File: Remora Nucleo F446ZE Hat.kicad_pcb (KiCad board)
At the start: 2 copper layers, 138 x 162 mm, 174 parts, among them J1 Conn_02x35_Odd_Even, J10 Conn_01x02_Socket, J11 Conn_01x04_Socket, J12 Conn_01x02_Socket, J13 Conn_01x04_Socket, J14 Conn_01x02_Socket, J15 Conn_01x04_Socket, J16 Conn_01x02_Socket, J17 Conn_01x04_Socket, J18 Conn_01x02_Socket, J19 Conn_01x04_Socket, J2 MSD-1-A, J20 Conn_01x04_Socket, J21 Conn_01x02_Socket, J23 Conn_01x04_Socket, J24 Conn_01x04_Socket, J25 Conn_01x04_Socket, J26 Conn_01x04_Socket, J27 Conn_01x02_Socket, J3 UART_TX, J4 Conn_02x35_Odd_Even, J5 24V Logic, J6 24V Peripheral, J7 Conn_01x04_Socket, J8 Conn_01x02_Socket, J9 Conn_01x04_Socket, SW1 SW_Push, U1 Wiznet W5500 Eval Module, U10 LTV-247, U11 LTV-247, U12 AM26LS31CDR, U13 LTV-247, U14 AM26LS31CDR, U19 LTV-247, U2 XL1509-12, U3 XL1509-5.0, U4 LTV-247, U5 AM26LS31CDR, U6 LTV-247, U7 LTV-247, U8 LTV-247, U9 LTV-247

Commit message: Layout work for PSUs
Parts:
- moved R10 411.1 mm to (229.9, 70.2), turned to 90 degrees
- moved D5 406.2 mm to (229.9, 65.3), turned to -90 degrees
- moved D6 368.5 mm to (269.2, 65.2), turned to -90 degrees
- moved J5 284.1 mm to (203.2, 68.2)
- moved C7 281.3 mm to (222.3, 68.2)
- moved U2 276.9 mm to (215.4, 80.0)
- moved C3 274.3 mm to (203.7, 78.6), turned to -90 degrees
- moved C5 266.1 mm to (209.4, 79.9), turned to -90 degrees
- moved JP1 263.7 mm to (223.6, 74.6)
- moved D3 261.7 mm to (214.0, 74.8)
- moved L1 259.2 mm to (214.1, 68.2)
- moved JP3 257.9 mm to (234.3, 66.0), turned to 180 degrees
- moved JP4 257.6 mm to (234.3, 70.4), turned to 180 degrees
- moved J6 255.9 mm to (242.2, 68.3)
- moved C8 247.6 mm to (261.7, 68.3)
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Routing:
- net +24V: track 0.00 -> 60.1 mm
- net VDD: track 0.00 -> 36.6 mm
- net Net-(JP1-A): track 0.00 -> 33.2 mm
- net Net-(JP2-A): track 0.00 -> 32.7 mm
- net Net-(D4-K): track 0.00 -> 13.8 mm
- net Net-(D3-K): track 0.00 -> 13.8 mm
- net +5VD: track 0.00 -> 6.85 mm
- net +12V: track 0.00 -> 6.82 mm
- net Net-(D6-A): track 0.00 -> 1.91 mm
- net Net-(D5-A): track 0.00 -> 1.91 mm
- net GNDREF: vias 9 -> 17
- net GNDPWR: vias 0 -> 9
- added copper zone on B.Cu, net GNDPWR
- added copper zone on F.Cu, net GNDPWR
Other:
- board text added: "24V Isolated"
- board text added: "24V Logic"

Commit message: Added Analog inputs, updates to readme re powering board from external supply
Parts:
- added C27: 100nF, Capacitor_SMD:C_1206_3216Metric_Pad1.33x1.80mm_HandSolder, F.Cu at (315.6, 112.9)
- added C28: 100nF, Capacitor_SMD:C_1206_3216Metric_Pad1.33x1.80mm_HandSolder, F.Cu at (315.6, 116.3)
- added C29: 100nF, Capacitor_SMD:C_1206_3216Metric_Pad1.33x1.80mm_HandSolder, F.Cu at (315.6, 119.6)
- added D7: 5.6V Zener, Package_TO_SOT_SMD:SOT-23, F.Cu at (327.0, 113.6)
- added D8: 5.6V Zener, Package_TO_SOT_SMD:SOT-23, F.Cu at (327.0, 118.3)
- added F10: PRG18BB330MB1RB, Fuse:Fuse_0603_1608Metric_Pad1.05x0.95mm_HandSolder, F.Cu at (331.6, 115.0)
- added F9: PRG18BB330MB1RB, Fuse:Fuse_0603_1608Metric_Pad1.05x0.95mm_HandSolder, F.Cu at (331.6, 112.5)
- added J19: Conn_01x04_Socket, Amphenol QT:QT04ADP83V0000G, F.Cu at (317.7, 104.1)
- added R80: 2K4, Resistor_SMD:R_1206_3216Metric_Pad1.30x1.75mm_HandSolder, F.Cu at (321.6, 112.9)
- added R81: 2K4, Resistor_SMD:R_1206_3216Metric_Pad1.30x1.75mm_HandSolder, F.Cu at (321.6, 116.2)
- added R82: 4K7, Resistor_SMD:R_1206_3216Metric_Pad1.30x1.75mm_HandSolder, F.Cu at (321.6, 119.5)
- added R83: 4K7, Resistor_SMD:R_1206_3216Metric_Pad1.30x1.75mm_HandSolder, F.Cu at (321.6, 122.8)
- added U15: MCP6042, Package_SO:SOIC-8_3.9x4.9mm_P1.27mm, F.Cu at (335.0, 128.1)
- J6: value 24V Peripheral -> 24V Isolated
- JP3: value Peripheral->Logic VDD Jumper -> Isolated->Logic VDD Jumper
- JP4: value Peripheral->Logic GND Jumper -> Isolated->Logic GND Jumper
- moved R1 361.0 mm to (159.7, 88.3), turned to 180 degrees
- moved D2 347.6 mm to (226.7, 105.8)
- moved J3 345.1 mm to (229.2, 110.5), turned to -90 degrees
- moved R2 315.1 mm to (214.0, 187.7), turned to -90 degrees
- moved R68 300.0 mm to (471.8, 304.4)
- moved R69 300.0 mm to (471.8, 307.7)
- moved R70 300.0 mm to (471.8, 311.0)
- moved R71 300.0 mm to (471.8, 314.4)
- moved R3 291.1 mm to (229.2, 105.8), turned to 90 degrees
- moved R79 285.5 mm to (525.9, 314.6)
- moved R77 282.3 mm to (525.9, 307.9)
- moved R78 280.6 mm to (525.9, 311.3)
- moved R75 279.1 mm to (525.9, 301.3)
- moved R76 277.4 mm to (525.9, 304.6)
- moved R73 276.0 mm to (525.9, 294.7)
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- renumbered C27 to C30, C29 to C32, J19 to J20, J20 to J21, J21 to J22, J23 to J24, J24 to J25, J25 to J26, J26 to J27, J27 to J28, R84 to R88, R85 to R89, R86 to R90, R87 to R91, U19 to U20
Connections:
- J4 pad 35: unconnected-(J4-Pin_35-Pad35) -> MCU_ANALOG_IN_0
- J4 pad 37: unconnected-(J4-Pin_37-Pad37) -> MCU_ANALOG_IN_1
- R32 pad 1: /Digital Inputs/Digital Input 4-7/INPUT4 -> +5VD
- R33 pad 1: /Digital Inputs/Digital Input 4-7/INPUT5 -> +5VD
- R34 pad 1: /Digital Inputs/Digital Input 4-7/INPUT6 -> +5VD
- R35 pad 1: /Digital Inputs/Digital Input 4-7/INPUT7 -> +5VD
- R40 pad 1: /Digital Inputs/Digital Input 8-11/INPUT8 -> +5VD
- R41 pad 1: /Digital Inputs/Digital Input 8-11/INPUT9 -> +5VD
- R42 pad 1: /Digital Inputs/Digital Input 8-11/INPUT10 -> +5VD
- R43 pad 1: /Digital Inputs/Digital Input 8-11/INPUT11 -> +5VD
- R44 pad 1: /Digital Inputs/Digital Input 12-15/INPUT12 -> +5VD
- R45 pad 1: /Digital Inputs/Digital Input 12-15/INPUT13 -> +5VD
- R46 pad 1: /Digital Inputs/Digital Input 12-15/INPUT14 -> +5VD
- R47 pad 1: /Digital Inputs/Digital Input 12-15/INPUT15 -> +5VD
- R88 pad 1: /Digital Inputs/Digital Input 0-3/INPUT0 -> +5VD
- R89 pad 1: /Digital Inputs/Digital Input 0-3/INPUT1 -> +5VD
- R90 pad 1: /Digital Inputs/Digital Input 0-3/INPUT2 -> +5VD
- R91 pad 1: /Digital Inputs/Digital Input 0-3/INPUT3 -> +5VD
- U10 pad 2: GNDPWR -> /Digital Inputs/Digital Input 12-15/INPUT12
- U10 pad 4: GNDPWR -> /Digital Inputs/Digital Input 12-15/INPUT13
- U10 pad 6: GNDPWR -> /Digital Inputs/Digital Input 12-15/INPUT14
- U10 pad 8: GNDPWR -> /Digital Inputs/Digital Input 12-15/INPUT15
- U20 pad 2: GNDPWR -> /Digital Inputs/Digital Input 0-3/INPUT0
- U20 pad 4: GNDPWR -> /Digital Inputs/Digital Input 0-3/INPUT1
- U20 pad 6: GNDPWR -> /Digital Inputs/Digital Input 0-3/INPUT2
- U20 pad 8: GNDPWR -> /Digital Inputs/Digital Input 0-3/INPUT3
- U7 pad 2: GNDPWR -> /Digital Inputs/Digital Input 4-7/INPUT4
- U7 pad 4: GNDPWR -> /Digital Inputs/Digital Input 4-7/INPUT5
- U7 pad 6: GNDPWR -> /Digital Inputs/Digital Input 4-7/INPUT6
- U7 pad 8: GNDPWR -> /Digital Inputs/Digital Input 4-7/INPUT7
- U9 pad 2: GNDPWR -> /Digital Inputs/Digital Input 8-11/INPUT8
- U9 pad 4: GNDPWR -> /Digital Inputs/Digital Input 8-11/INPUT9
- U9 pad 6: GNDPWR -> /Digital Inputs/Digital Input 8-11/INPUT10
- U9 pad 8: GNDPWR -> /Digital Inputs/Digital Input 8-11/INPUT11
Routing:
- net +3V3: vias 1 -> 0
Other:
- board text added: "Nucleo CNC controller V1"
- board text added: "RESET"
- board text removed: "Remora Nucleo CNC controller V1"

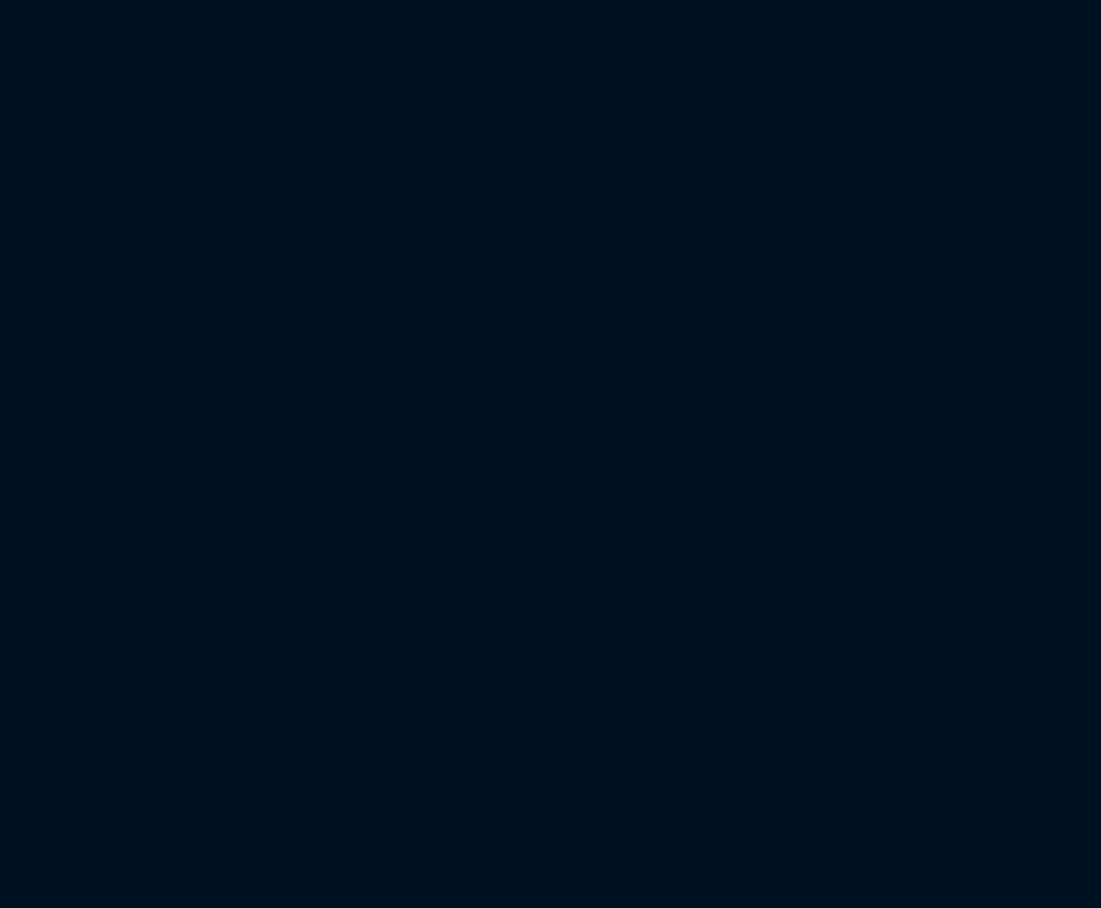
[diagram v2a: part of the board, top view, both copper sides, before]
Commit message: Finalised Spindle DAC, working as expected
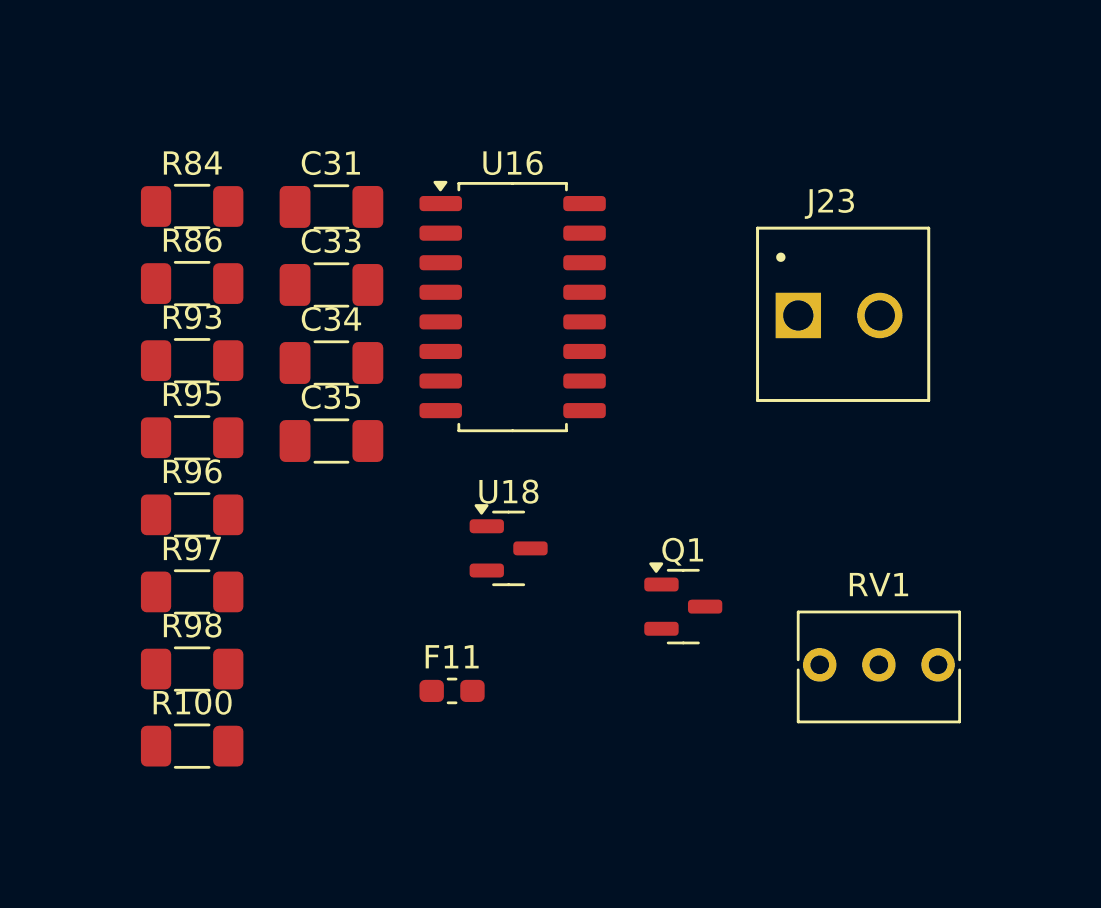
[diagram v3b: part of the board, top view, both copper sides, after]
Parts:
- added C31: 100nF, Capacitor_SMD:C_1206_3216Metric_Pad1.33x1.80mm_HandSolder, F.Cu at (319.0, 37.8)
- added C33: 100nF, Capacitor_SMD:C_1206_3216Metric_Pad1.33x1.80mm_HandSolder, F.Cu at (319.0, 41.2)
- added C34: 100nF, Capacitor_SMD:C_1206_3216Metric_Pad1.33x1.80mm_HandSolder, F.Cu at (319.0, 44.5)
- added C35: 100nF, Capacitor_SMD:C_1206_3216Metric_Pad1.33x1.80mm_HandSolder, F.Cu at (319.0, 47.9)
- added F11: PRG18BB330MB1RB, Fuse:Fuse_0603_1608Metric_Pad1.05x0.95mm_HandSolder, F.Cu at (324.1, 58.6)
- added J23: Spindle Out, EBWA_02_A:ADAMTECH_EBWA-02-A, F.Cu at (340.8, 42.5)
- added Q1: BC847, Package_TO_SOT_SMD:SOT-23, F.Cu at (334.1, 55.0)
- added R100: 4K7, Resistor_SMD:R_1206_3216Metric_Pad1.30x1.75mm_HandSolder, F.Cu at (313.0, 61.0)
- added R84: 180R, Resistor_SMD:R_1206_3216Metric_Pad1.30x1.75mm_HandSolder, F.Cu at (313.0, 37.8)
- added R86: 1K2, Resistor_SMD:R_1206_3216Metric_Pad1.30x1.75mm_HandSolder, F.Cu at (313.0, 41.1)
- added R93: 10K, Resistor_SMD:R_1206_3216Metric_Pad1.30x1.75mm_HandSolder, F.Cu at (313.0, 44.4)
- added R95: 1K2, Resistor_SMD:R_1206_3216Metric_Pad1.30x1.75mm_HandSolder, F.Cu at (313.0, 47.8)
- added R96: 4K7, Resistor_SMD:R_1206_3216Metric_Pad1.30x1.75mm_HandSolder, F.Cu at (313.0, 51.1)
- added R97: 4K7, Resistor_SMD:R_1206_3216Metric_Pad1.30x1.75mm_HandSolder, F.Cu at (313.0, 54.4)
- added R98: 4K7, Resistor_SMD:R_1206_3216Metric_Pad1.30x1.75mm_HandSolder, F.Cu at (313.0, 57.7)
- added RV1: 10K 25 turn trimpot, Potentiometer_THT:Potentiometer_Bourns_3266Y_Vertical, F.Cu at (345.0, 57.5)
- added U16: LTV-247, Package_SO:SOP-16_4.4x10.4mm_P1.27mm, F.Cu at (326.7, 42.1)
- added U18: TL431A, Package_TO_SOT_SMD:SOT-23, F.Cu at (326.6, 52.5)
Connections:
- net test renamed Net-(D7-K)
- J4 pad 43: unconnected-(J4-Pin_43-Pad43) -> MCU_SPINDLE

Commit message: Testing multi channel layout, test layout for stepper drivers
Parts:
- added C36: 100nF, Capacitor_SMD:C_1206_3216Metric_Pad1.33x1.80mm_HandSolder, F.Cu at (235.9, -36.7)
- added C37: 100nF, Capacitor_SMD:C_1206_3216Metric_Pad1.33x1.80mm_HandSolder, F.Cu at (235.9, -33.4)
- added C38: 100nF, Capacitor_SMD:C_1206_3216Metric_Pad1.33x1.80mm_HandSolder, F.Cu at (235.9, -30.0)
- added J20: Conn_01x04_Socket, Amphenol QT:QT04ADP83V0000G, F.Cu at (215.4, -45.5)
- added J21: Conn_01x02_Socket, Amphenol QT:QT02ADP83V0000G, F.Cu at (215.4, -29.4)
- added R84: 1K2, Resistor_SMD:R_1206_3216Metric_Pad1.30x1.75mm_HandSolder, F.Cu at (236.4, -52.8)
- added R85: 1K2, Resistor_SMD:R_1206_3216Metric_Pad1.30x1.75mm_HandSolder, F.Cu at (236.4, -49.5)
- added R86: 1K2, Resistor_SMD:R_1206_3216Metric_Pad1.30x1.75mm_HandSolder, F.Cu at (236.4, -46.2)
- added U16: LTV-247, Package_SO:SOP-16_4.4x10.4mm_P1.27mm, F.Cu at (228.2, -32.4)
- moved J15 134.2 mm to (568.5, 334.2)
- moved J16 134.2 mm to (568.5, 354.2)
- moved J17 133.3 mm to (588.0, 357.4)
- moved J18 133.3 mm to (588.0, 337.4)
- moved C21 130.2 mm to (591.7, 366.0), turned to 180 degrees
- moved R68 125.8 mm to (580.5, 367.7), turned to 180 degrees
- moved R69 125.8 mm to (580.5, 371.0), turned to 180 degrees
- moved R70 125.8 mm to (580.5, 374.3), turned to 180 degrees
- moved R71 125.8 mm to (580.5, 377.6), turned to 180 degrees
- moved R64 121.6 mm to (566.3, 367.7)
- moved R65 121.6 mm to (566.3, 371.0)
- moved R66 121.6 mm to (566.3, 374.3)
- moved R67 121.6 mm to (566.3, 377.6)
- moved C15 121.6 mm to (591.9, 287.1), turned to 180 degrees
- moved U13 121.6 mm to (573.5, 372.6)
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- renumbered C33 to C32, C35 to C33, C32 to C35, J20 to J22, J21 to J23, J22 to J24, J23 to J25, J24 to J26, J25 to J27, J26 to J28, J27 to J29, J28 to J30, R84 to R87, R97 to R88, R96 to R89, R98 to R90, R93 to R91, R95 to R92, R100 to R93, R86 to R94, R88 to R95, R89 to R96, R90 to R97, R91 to R98, U16 to U17, U20 to U19
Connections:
- J4 pad 19: unconnected-(J4-Pin_19-Pad19) -> QEI_B
- J4 pad 21: MCU_DIGITAL_OUT_5 -> unconnected-(J4-Pin_21-Pad21)
- J4 pad 23: MCU_DIGITAL_OUT_4 -> QEI_Z
- J4 pad 25: unconnected-(J4-Pin_25-Pad25) -> MCU_DIGITAL_OUT_5
- J4 pad 27: unconnected-(J4-Pin_27-Pad27) -> MCU_DIGITAL_OUT_4
- J4 pad 4: unconnected-(J4-Pin_4-Pad4) -> QEI_A
- R96 pad 2: Net-(R89-Pad2) -> Net-(R96-Pad2)
- R97 pad 2: Net-(R90-Pad2) -> Net-(R97-Pad2)
- R98 pad 2: Net-(R91-Pad2) -> Net-(R98-Pad2)
- U17 pad 11: (no net) -> GNDREF
- U17 pad 12: (no net) -> MCU_DIGITAL_IN_2
- U17 pad 13: (no net) -> GNDREF
- U17 pad 14: (no net) -> MCU_DIGITAL_IN_1
- U17 pad 3: (no net) -> Net-(R96-Pad2)
- U17 pad 4: (no net) -> /Digital Inputs/Digital Input 0-3/INPUT1
- U17 pad 5: (no net) -> Net-(R97-Pad2)
- U17 pad 6: (no net) -> /Digital Inputs/Digital Input 0-3/INPUT2
- U19 pad 10: MCU_DIGITAL_IN_3 -> (no net)
- U19 pad 11: GNDREF -> (no net)
- U19 pad 12: MCU_DIGITAL_IN_2 -> (no net)
- U19 pad 13: GNDREF -> (no net)
- U19 pad 14: MCU_DIGITAL_IN_1 -> (no net)
- U19 pad 3: Net-(R89-Pad2) -> (no net)
- U19 pad 4: /Digital Inputs/Digital Input 0-3/INPUT1 -> (no net)
- U19 pad 5: Net-(R90-Pad2) -> (no net)
- U19 pad 6: /Digital Inputs/Digital Input 0-3/INPUT2 -> (no net)
- U19 pad 7: Net-(R91-Pad2) -> (no net)
- U19 pad 8: /Digital Inputs/Digital Input 0-3/INPUT3 -> (no net)
- U19 pad 9: GNDREF -> (no net)
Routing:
- net +5VD: track 6.85 -> 398.7 mm
- net /Z and A Stepper Drivers/Z_STEP+: track 0.00 -> 57.8 mm, vias 0 -> 1
- net /B and C Stepper Drivers/B_STEP+: track 0.00 -> 57.8 mm, vias 0 -> 1
- net /X and Y Stepper Drivers/X_STEP+: track 0.00 -> 57.8 mm, vias 0 -> 1
- net /Z and A Stepper Drivers/A_DIR-: track 0.00 -> 56.4 mm, vias 0 -> 1
- net /X and Y Stepper Drivers/Y_DIR-: track 0.00 -> 56.4 mm, vias 0 -> 1
- net /B and C Stepper Drivers/C_DIR-: track 0.00 -> 56.4 mm, vias 0 -> 1
- net /X and Y Stepper Drivers/X_DIR+: track 0.00 -> 53.7 mm, vias 0 -> 1
- net /Z and A Stepper Drivers/Z_DIR+: track 0.00 -> 53.7 mm, vias 0 -> 1
- net /B and C Stepper Drivers/B_DIR+: track 0.00 -> 53.7 mm, vias 0 -> 1
- net /X and Y Stepper Drivers/X_STEP-: track 0.00 -> 53.1 mm, vias 0 -> 1
- net /Z and A Stepper Drivers/Z_STEP-: track 0.00 -> 53.1 mm, vias 0 -> 1
- net /B and C Stepper Drivers/B_STEP-: track 0.00 -> 53.1 mm, vias 0 -> 1
- net /X and Y Stepper Drivers/Y_DIR+: track 0.00 -> 50.8 mm, vias 0 -> 1
- net /Z and A Stepper Drivers/A_DIR+: track 0.00 -> 50.8 mm, vias 0 -> 1
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
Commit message: Layout for stepper drivers and digital inputs
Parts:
- removed C1: 100nF, Capacitor_SMD:C_1206_3216Metric_Pad1.33x1.80mm_HandSolder
- removed C2: 10uF, Capacitor_SMD:C_1206_3216Metric_Pad1.33x1.80mm_HandSolder
- removed J2: MSD-1-A, MSD1A Symbols:MSD1A
- removed R4, R5, R6, R7, R8, R9: 4K7, Resistor_SMD:R_1206_3216Metric_Pad1.30x1.75mm_HandSolder
- removed the R95 at (509.4, 52.7)
- removed the R96 at (509.4, 56.0)
- removed the R97 at (509.4, 59.3)
- removed the R98 at (509.4, 62.6)
- removed RP1: Raspberry_Pi_Header, RPI3FootPrint:raspberrypi_2_3
- removed the U19 at (517.1, 57.0)
- added R48: 180R, Resistor_SMD:R_1206_3216Metric_Pad1.30x1.75mm_HandSolder, F.Cu at (175.1, 209.1)
- added R49: 180R, Resistor_SMD:R_1206_3216Metric_Pad1.30x1.75mm_HandSolder, F.Cu at (172.6, 209.1)
- added R50: 180R, Resistor_SMD:R_1206_3216Metric_Pad1.30x1.75mm_HandSolder, F.Cu at (175.1, 204.0)
- added R51: 180R, Resistor_SMD:R_1206_3216Metric_Pad1.30x1.75mm_HandSolder, F.Cu at (172.6, 204.0)
- added U11: LTV-247, Package_SO:SOP-16_4.4x10.4mm_P1.27mm, F.Cu at (167.1, 207.0)
- moved U9 382.9 mm to (167.1, 187.5), turned to 180 degrees
- moved U7 377.2 mm to (167.1, 153.2), turned to 180 degrees
- moved C22 374.9 mm to (252.9, 207.3), turned to 180 degrees
- moved C18 373.2 mm to (243.9, 160.6), turned to -90 degrees
- moved R41 372.1 mm to (172.6, 189.6), turned to 90 degrees
- moved J16 371.9 mm to (235.4, 188.9), turned to 180 degrees
- moved R40 371.2 mm to (175.1, 189.6), turned to 90 degrees
- moved R43 367.3 mm to (172.6, 184.5), turned to -90 degrees
- moved R42 366.4 mm to (175.1, 184.5), turned to -90 degrees
- moved R33 366.0 mm to (172.6, 155.4), turned to 90 degrees
- moved R32 364.9 mm to (175.1, 155.4), turned to 90 degrees
- moved R83 363.1 mm to (265.9, 200.8), turned to -90 degrees
- moved R35 361.7 mm to (172.6, 150.3), turned to -90 degrees
- moved R34 360.6 mm to (175.1, 150.3), turned to -90 degrees
- moved R81 360.5 mm to (269.9, 200.8), turned to -90 degrees
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- renumbered C36 to C30, C37 to C31, C38 to C32, C30 to C33, C31 to C34, C32 to C35, C33 to C36, C34 to C37, C35 to C38, R48 to R52, R49 to R53, R50 to R54, R51 to R55, R52 to R56, R53 to R57, R54 to R58, R55 to R59, R56 to R60, R57 to R61, R58 to R62, R59 to R63, R60 to R64, R61 to R65, R62 to R66, R63 to R67, R64 to R68, R65 to R69, R66 to R70, R67 to R71, R68 to R72, R69 to R73, R70 to R74, R71 to R75, R72 to R76, R73 to R77, R74 to R78, R75 to R79, R76 to R80, R77 to R81, R78 to R82, R79 to R83, R80 to R84, R81 to R85, R82 to R86, R83 to R87, R84 to R88, R85 to R89, R86 to R90, R87 to R91, R88 to R92, R89 to R93, R90 to R94, R91 to R95, R92 to R96, R93 to R97, R94 to R98, U11 to U12, U12 to U13, U13 to U14, U14 to U15, U15 to U16, U16 to U17, U17 to U18, U18 to U19
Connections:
- U17 pad 10: MCU_DIGITAL_IN_3 -> (no net)
- U17 pad 7: Net-(R98-Pad2) -> (no net)
- U17 pad 8: /Digital Inputs/Digital Input 0-3/INPUT3 -> (no net)
- U17 pad 9: GNDREF -> (no net)
- U18 pad 11: GNDREF -> (no net)
- U18 pad 12: MCU_DIGITAL_IN_2 -> (no net)
- U18 pad 13: GNDREF -> (no net)
- U18 pad 14: MCU_DIGITAL_IN_1 -> (no net)
- U18 pad 3: Net-(R96-Pad2) (its old number) -> (no net)
- U18 pad 4: /Digital Inputs/Digital Input 0-3/INPUT1 -> (no net)
- U18 pad 5: Net-(R97-Pad2) -> (no net)
- U18 pad 6: /Digital Inputs/Digital Input 0-3/INPUT2 -> (no net)
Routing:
- net +5VD: track 398.7 -> 6.85 mm
- net /Z and A Stepper Drivers/Z_STEP+: track 57.8 -> 0.00 mm, vias 1 -> 0
- net /B and C Stepper Drivers/B_STEP+: track 57.8 -> 0.00 mm, vias 1 -> 0
- net /X and Y Stepper Drivers/X_STEP+: track 57.8 -> 0.00 mm, vias 1 -> 0
- net /Z and A Stepper Drivers/A_DIR-: track 56.4 -> 0.00 mm, vias 1 -> 0
- net /X and Y Stepper Drivers/Y_DIR-: track 56.4 -> 0.00 mm, vias 1 -> 0
- net /B and C Stepper Drivers/C_DIR-: track 56.4 -> 0.00 mm, vias 1 -> 0
- net /X and Y Stepper Drivers/X_DIR+: track 53.7 -> 0.00 mm, vias 1 -> 0
- net /Z and A Stepper Drivers/Z_DIR+: track 53.7 -> 0.00 mm, vias 1 -> 0
- net /B and C Stepper Drivers/B_DIR+: track 53.7 -> 0.00 mm, vias 1 -> 0
- net /X and Y Stepper Drivers/X_STEP-: track 53.1 -> 0.00 mm, vias 1 -> 0
- net /Z and A Stepper Drivers/Z_STEP-: track 53.1 -> 0.00 mm, vias 1 -> 0
- net /B and C Stepper Drivers/B_STEP-: track 53.1 -> 0.00 mm, vias 1 -> 0
- net /X and Y Stepper Drivers/Y_DIR+: track 50.8 -> 0.00 mm, vias 1 -> 0
- net /Z and A Stepper Drivers/A_DIR+: track 50.8 -> 0.00 mm, vias 1 -> 0
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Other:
- board text added: "© 2026 Ben Jacobson JLCJLCJLCJLC"
- board text removed: "© 2025 Ben Jacobson JLCJLCJLCJLC"

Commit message: Switched terminal footprints over to a finer pitch. Corrected an issue with component reference values preventing proper use of multi channel rule areas. Component references for 4 channel optos are more straightforward as a result
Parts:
- removed the U18 at (326.7, 42.1)
- J10, J12, J14, J16, J18, J21, J24, J30, J8: footprint Amphenol QT:QT02ADP83V0000G -> 691412120002B:691412120002B
- J11, J13, J15, J17, J19, J20, J22, J23, J26, J27, J28, J29, J7, J9: footprint Amphenol QT:QT04ADP83V0000G -> 691412120004B:691412120004B
- J25, J5, J6: footprint EBWA_02_A:ADAMTECH_EBWA-02-A -> 691412120002B:691412120002B
- moved U6 592.5 mm to (57.9, 174.1)
- moved C33 577.6 mm to (50.6, 248.0)
- moved F5 577.6 mm to (77.7, 208.9)
- moved F6 577.6 mm to (77.7, 211.4)
- moved F7 577.6 mm to (77.7, 213.9)
- moved F8 577.6 mm to (77.7, 216.4)
- moved R28 577.6 mm to (59.4, 225.6)
- moved R29 577.6 mm to (59.4, 228.9)
- moved R30 577.6 mm to (59.4, 232.2)
- moved R31 577.6 mm to (59.4, 235.5)
- moved F1 577.6 mm to (99.5, 208.9)
- moved F2 577.6 mm to (99.5, 211.4)
- moved F3 577.6 mm to (99.5, 213.9)
- moved F4 577.6 mm to (99.5, 216.4)
- moved R36 577.6 mm to (51.4, 225.6)
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- renumbered U19 to U18
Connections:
- U17 pad 1: Net-(R88-Pad1) -> Net-(R91-Pad2)
- U17 pad 10: (no net) -> QEI_Z
- U17 pad 12: QEI_Z -> QEI_B
- U17 pad 14: QEI_B -> QEI_A
- U17 pad 15: GNDREF -> Net-(R92-Pad1)
- U17 pad 16: QEI_A -> Net-(Q1-C)
- U17 pad 2: /Encoder Inputs/QEI_A_IN -> GNDREF
- U17 pad 3: Net-(R89-Pad1) -> Net-(R88-Pad1)
- U17 pad 4: /Encoder Inputs/QEI_B_IN -> /Encoder Inputs/QEI_A_IN
- U17 pad 5: Net-(R90-Pad1) -> Net-(R89-Pad1)
- U17 pad 6: /Encoder Inputs/QEI_Z_IN -> /Encoder Inputs/QEI_B_IN
- U17 pad 7: (no net) -> Net-(R90-Pad1)
- U17 pad 8: (no net) -> /Encoder Inputs/QEI_Z_IN
- U17 pad 9: (no net) -> GNDREF
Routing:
- net VDD: track 36.6 -> 25.7 mm
- net +24V: track 60.1 -> 61.0 mm
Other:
- board text removed: "Raspberry Pi"
